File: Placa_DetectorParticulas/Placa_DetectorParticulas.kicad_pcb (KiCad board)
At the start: 4 copper layers, 80 x 79 mm, 177 parts, among them J1 Conn_02x08_Odd_Even, J2 Conn_02x08_Odd_Even, J3 Conn_02x08_Odd_Even, J4 Conn_02x08_Odd_Even, Q1 BSS123, Q2 BSS123, U1 max1932etc+T, U10 SN74LV1T04QDCKRQ1, U11 74LVC2G00DP_125, U12 SN74LV1T04QDCKRQ1, U13 74LVC2G00DP_125, U14 TMP100AQDBVRQ1, U18 NXS0108BQ-Q100X, U19 NXB0108BQ-Q100X, U2 OPA855QDSGRQ1, U20 max1932etc+T, U21 ADR5044WBRTZ-R7, U22 INA148QDRQ1, U23 TSZ122IQ2T, U24 INA148QDRQ1, U25 ADR5044WBRTZ-R7, U26 DAC8551AQDGKRQ1, U27 ADR5041WBRTZ-R7, U28 DAC8551AQDGKRQ1, U3 TSZ122IQ2T, U4 OPA855QDSGRQ1, U5 TSZ122IQ2T, U6 TS3011IYQ3T, U7 TS3011IYQ3T, U8 MCP4561T-104E/MF, U9 TSZ122IQ2T

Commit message: Dual Pot added.
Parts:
- removed C24: 100nF, Capacitor_SMD:C_0805_2012Metric
- removed U8: MCP4561T-104E/MF, 0A_MCP4561T_103E_MF:DFN8_3x3MC_MCH
- added C57: 100nF, Capacitor_SMD:C_0805_2012Metric, B.Cu at (119.8, 108.2)
- added R79: 1k, Resistor_SMD:R_0805_2012Metric, B.Cu at (119.8, 98.2)
- added R80: 0, Resistor_SMD:R_0805_2012Metric, B.Cu at (126.0, 109.5)
- added R81: 0, Resistor_SMD:R_0805_2012Metric, B.Cu at (124.1, 109.5)
- added U29: MCP4661T-104E/ML, 0A_MCP4661T_104E_ML:QFN16_4x4MC_MCH, B.Cu at (122.0, 104.4)
- C48, C49: value 1uF -> 100nF
- R16: value 12k -> 0
- R4: value 6.8k -> 4.7k
- R72, R73: value 1k -> 470
- moved R4 7.70 mm to (126.9, 105.6)
- moved U21 7.68 mm to (126.3, 101.2)
- moved R32 0.98 mm to (122.1, 98.2), turned to 90 degrees
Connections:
- net V3.5REF renamed V3.8REF
- R24 pad 1: VREF -> VREF1
- R27 pad 1: VREF -> VREF2
- U9 pad 1: Net-(U9-IN1-) -> VREF1
- U9 pad 2: Net-(U9-IN1-) -> VREF1
- U9 pad 5: Net-(U9-IN1-) -> Net-(U9-IN2+)
- U9 pad 6: VREF -> VREF2
- U9 pad 7: VREF -> VREF2
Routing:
- net VREF: track 45.6 -> 0.00 mm, vias 2 -> 0
- net VREF1: track 0.00 -> 43.2 mm, vias 0 -> 2
- net VREF2: track 0.00 -> 31.5 mm
- net Net-(U9-IN1-): track 15.3 -> 0.00 mm, vias 2 -> 0
- net GND: track 201.3 -> 212.3 mm
- net V0.6REF: track 126.0 -> 132.4 mm, vias 4 -> 3
- net +5V: track 139.3 -> 145.2 mm
- net Net-(U9-IN2+): track 0.00 -> 5.19 mm
- net Net-(U29-*WP): track 0.00 -> 5.14 mm
- net Net-(U29-P1W): track 0.00 -> 4.17 mm
- net Net-(U29-P0W): track 2.53 -> 5.13 mm
- net I2C5V_SDA: track 119.5 -> 117.3 mm
- net Net-(U21-NC): track 10.0 -> 11.6 mm, vias 0 -> 2
- net I2C5V_SCL: track 119.7 -> 121.2 mm
- net Net-(U9-IN1+): track 2.31 -> 1.76 mm

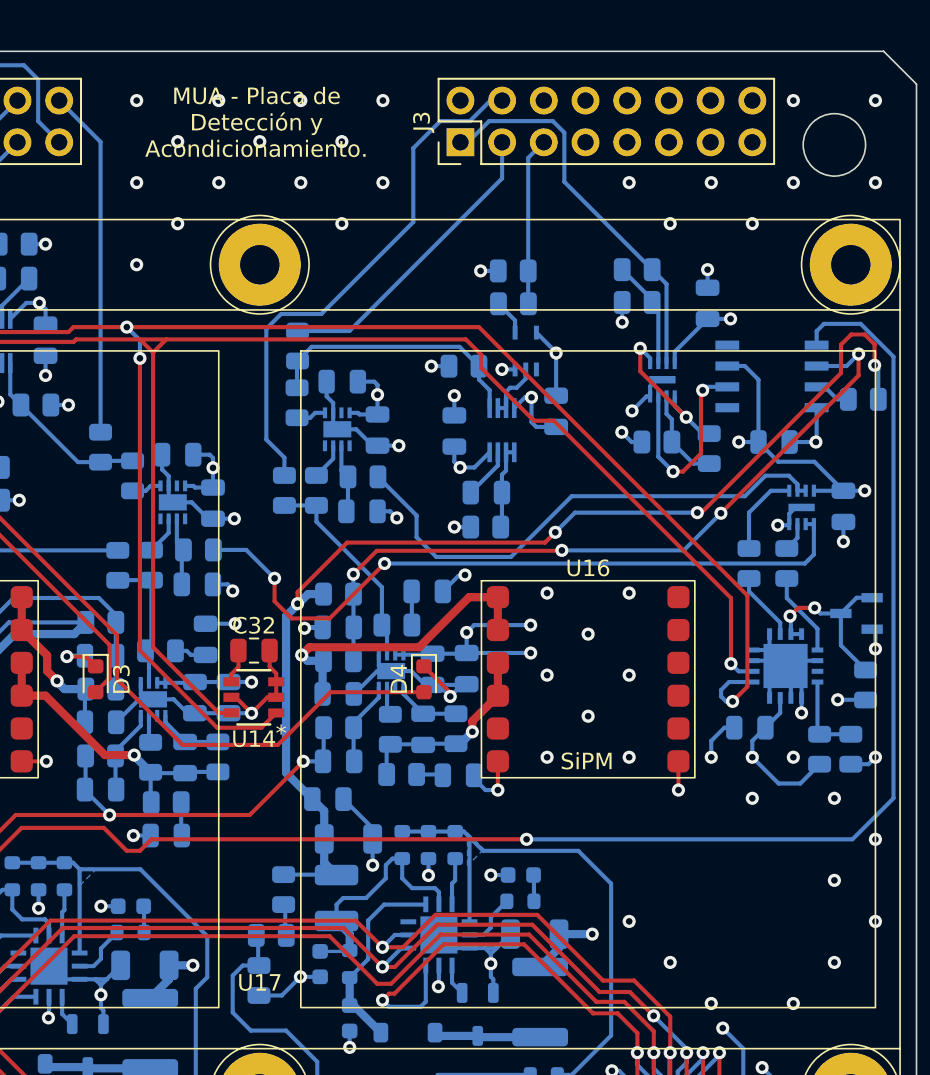
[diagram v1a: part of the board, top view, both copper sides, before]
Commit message: Added hysteresis in comparator.
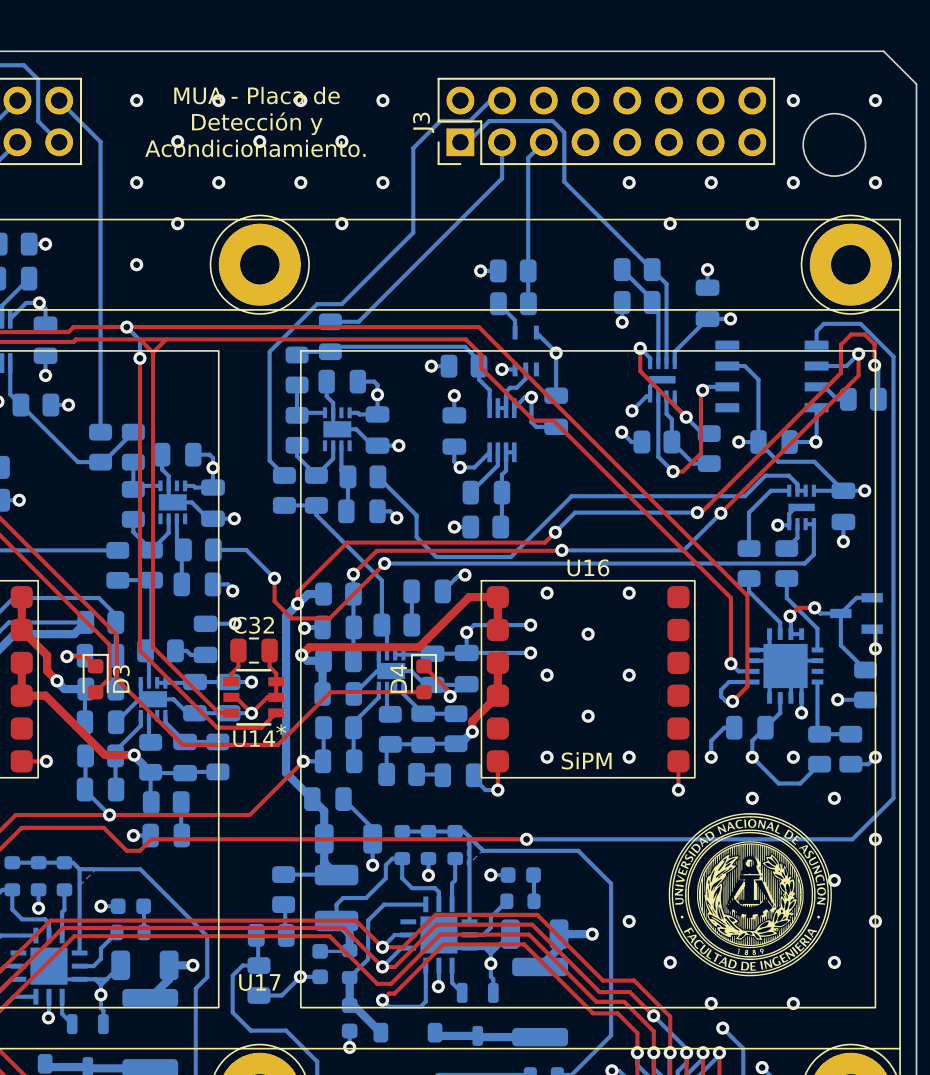
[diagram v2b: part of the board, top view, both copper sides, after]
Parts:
- added G***: LOGO, LOGO:Logo_FIUNA, F.Cu at (119.9, 118.4)
- added R82: 100k, Resistor_SMD:R_0805_2012Metric, B.Cu at (82.3, 94.6)
- added R83: 100k, Resistor_SMD:R_0805_2012Metric, B.Cu at (92.3, 90.1)
- moved R66 2.08 mm to (94.3, 84.4)
- moved R29 2.00 mm to (92.3, 86.4)
- moved R26 1.75 mm to (82.3, 91.1)
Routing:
- net Net-(U6-IN+): track 2.34 -> 4.67 mm
- net Net-(U7-IN+): track 2.23 -> 4.56 mm
- net PULSO2_FOUT5V: track 18.5 -> 16.3 mm
- net Net-(U7-OUT): track 1.82 -> 3.61 mm
- net Net-(U6-OUT): track 1.82 -> 3.40 mm
- net PULSO2_COMP: track 16.4 -> 14.8 mm
- net PULSO1_COMP: track 11.1 -> 11.9 mm
- net PULSO2_SENSE: track 32.1 -> 31.4 mm
